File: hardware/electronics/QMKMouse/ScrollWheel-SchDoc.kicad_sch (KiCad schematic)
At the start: 8 parts

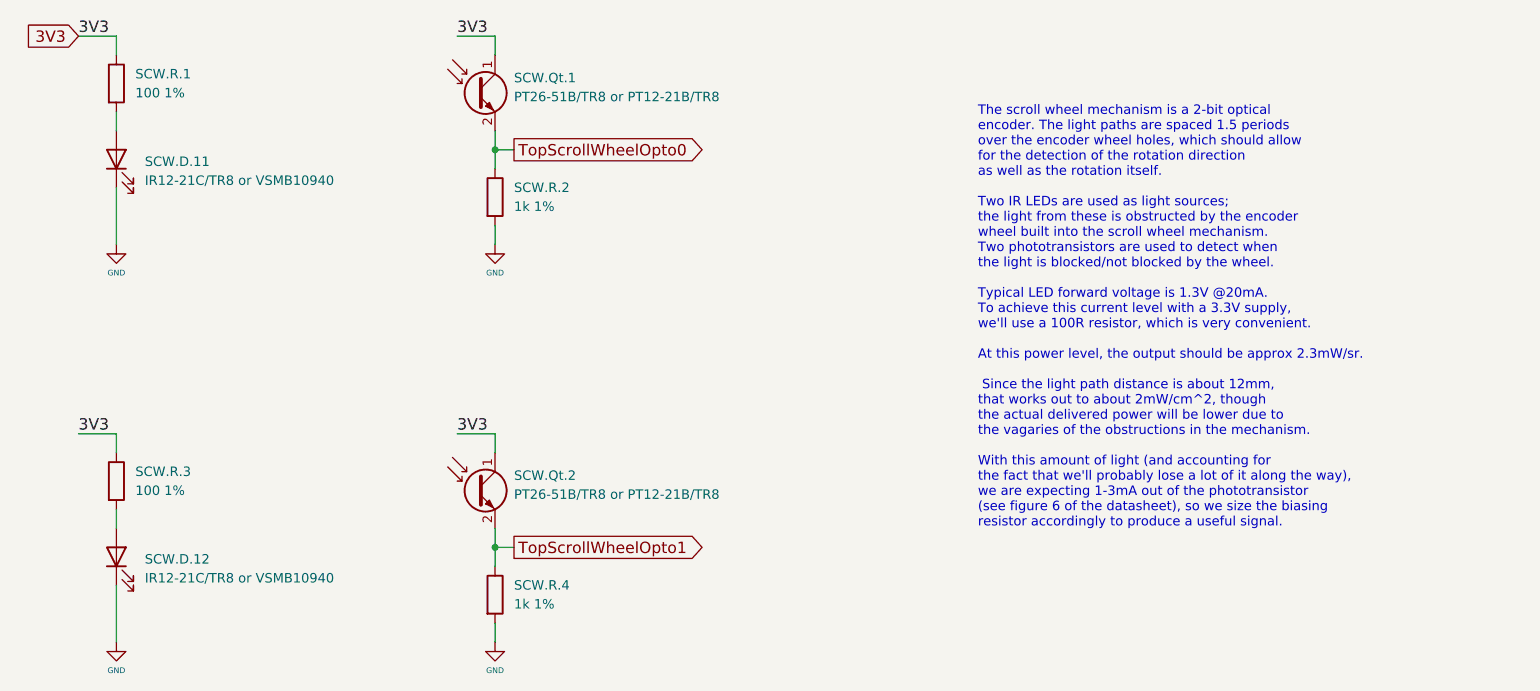
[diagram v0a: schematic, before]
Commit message: update schematic from PCB; sync netlist and fix some symbol orientations; also fix LED symbol
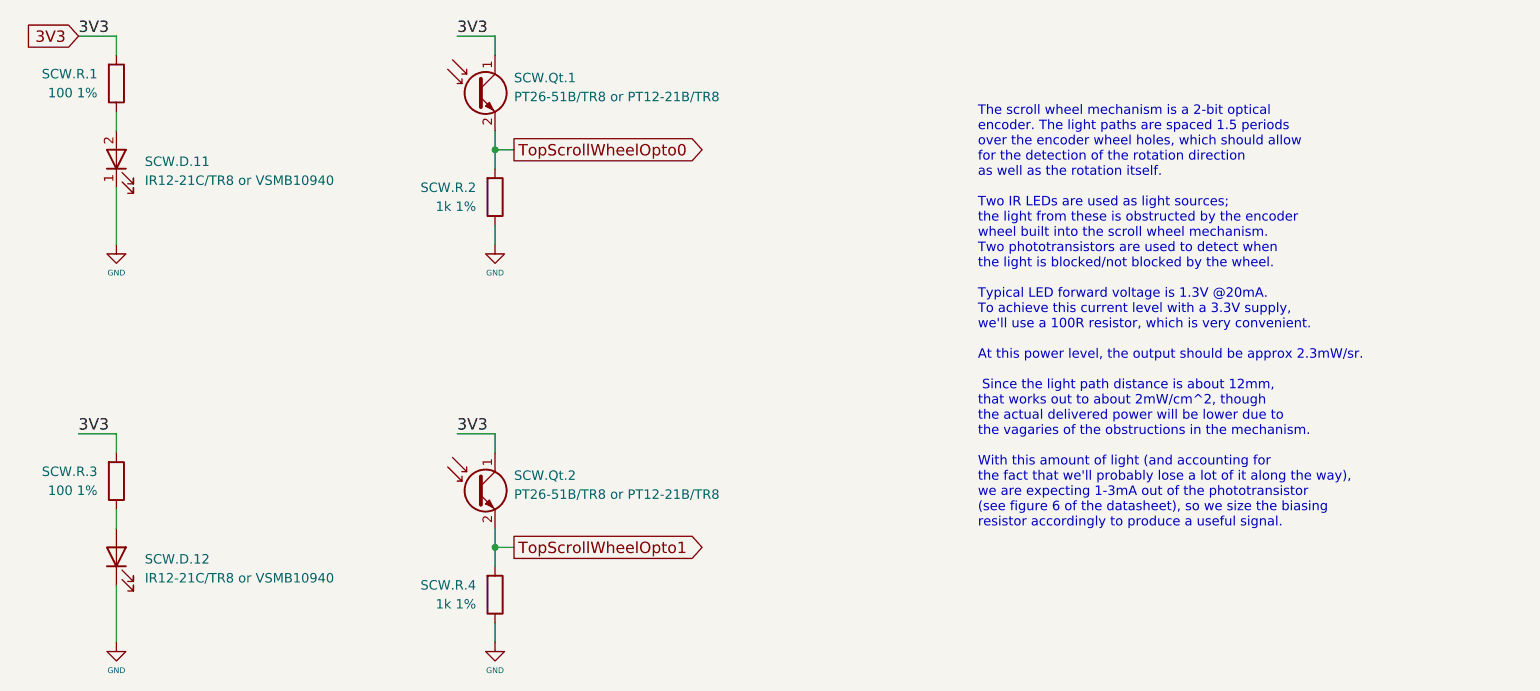
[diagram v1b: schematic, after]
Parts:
- SCW.D.11, SCW.D.12: footprint Mouse_Parts:Infrared emitter - VSMB10940 -> LEDs.PcbLib:IR12-21C/TR8
- SCW.Qt.1, SCW.Qt.2: footprint Mouse_Parts:Photo transistor - PT12-21B-TR8 -> OptoElectronics.PcbLib:PT26-51B/TR8
- SCW.R.1, SCW.R.2, SCW.R.3, SCW.R.4: footprint Resistor_SMD:R_0805_2012Metric -> Chip_Passives.PcbLib:0805
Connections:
- net 3V3: now also SCW.R.1.2, SCW.R.3.2; no longer SCW.R.1.1, SCW.R.3.1
- net GND: now also SCW.R.2.1, SCW.R.4.1; no longer SCW.R.2.2, SCW.R.4.2
- net TopScrollWheelOpto0: now also SCW.R.2.2; no longer SCW.R.2.1
- net TopScrollWheelOpto1: now also SCW.R.4.2; no longer SCW.R.4.1
- net at SCW.D.12.2 (A): now also SCW.R.3.1; no longer SCW.R.3.2
- net at SCW.D.11.2 (A): now also SCW.R.1.1; no longer SCW.R.1.2
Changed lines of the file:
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@@
     (pin "1")
   )
-  (symbol (lib_id "Device:R") (at 82.55 116.84 0) (unit 1)
+  (symbol (lib_id "Device:R") (at 82.55 116.84 0) (mirror x) (unit 1)
     (in_bom yes) (on_board yes) (fields_autoplaced)
-    (property "Reference" "SCW.R.3" (id 0) (at 85.09 115.5699 0)
-      (effects (font (size 1.27 1.27)) (justify left))
+    (property "Reference" "SCW.R.3" (id 0) (at 80.01 115.5699 0)
+      (effects (font (size 1.27 1.27)) (justify right))
     )
-    (property "Value" "100 1%" (id 1) (at 85.09 118.1099 0)
-      (effects (font (size 1.27 1.27)) (justify left))
+    (property "Value" "100 1%" (id 1) (at 80.01 118.1099 0)
+      (effects (font (size 1.27 1.27)) (justify right))
     )
-    (property "Footprint" "Resistor_SMD:R_0805_2012Metric" (id 2) (at 80.772 116.84 90)
+    (property "Footprint" "Chip_Passives.PcbLib:0805" (id 2) (at 80.772 116.84 90)
       (effects (font (size 1.27 1.27)) hide)
     )
@@
       (effects (font (size 1.27 1.27)) (justify right))
     )
-    (property "Footprint" "Mouse_Parts:Infrared emitter - VSMB10940" (id 2) (at 82.55 127 0)
+    (property "Footprint" "LEDs.PcbLib:IR12-21C{slash}TR8" (id 2) (at 82.55 127 0)
       (effects (font (size 1.27 1.27)) hide)
     )
@@
       (effects (font (size 1.27 1.27)) (justify left))
     )
-    (property "Footprint" "Mouse_Parts:Photo transistor - PT12-21B-TR8" (id 2) (at 135.89 115.57 0)
+    (property "Footprint" "OptoElectronics.PcbLib:PT26-51B{slash}TR8" (id 2) (at 135.89 115.57 0)
       (effects (font (size 1.27 1.27)) hide)
     )
@@
     (pin "2")
   )
-  (symbol (lib_id "Device:R") (at 82.55 63.5 0) (unit 1)
+  (symbol (lib_id "Device:R") (at 82.55 63.5 0) (mirror x) (unit 1)
     (in_bom yes) (on_board yes) (fields_autoplaced)
-    (property "Reference" "SCW.R.1" (id 0) (at 85.09 62.2299 0)
-      (effects (font (size 1.27 1.27)) (justify left))
+    (property "Reference" "SCW.R.1" (id 0) (at 80.01 62.2299 0)
+      (effects (font (size 1.27 1.27)) (justify right))
     )
-    (property "Value" "100 1%" (id 1) (at 85.09 64.7699 0)
-      (effects (font (size 1.27 1.27)) (justify left))
+    (property "Value" "100 1%" (id 1) (at 80.01 64.7699 0)
+      (effects (font (size 1.27 1.27)) (justify right))
     )
-    (property "Footprint" "Resistor_SMD:R_0805_2012Metric" (id 2) (at 80.772 63.5 90)
+    (property "Footprint" "Chip_Passives.PcbLib:0805" (id 2) (at 80.772 63.5 90)
       (effects (font (size 1.27 1.27)) hide)
     )
@@
     (pin "2")
   )
-  (symbol (lib_id "Device:LED") (at 82.55 73.66 90) (unit 1)
+  (symbol (lib_name "LED_1") (lib_id "Device:LED") (at 82.55 73.66 90) (unit 1)
     (in_bom yes) (on_board yes) (fields_autoplaced)
     (property "Reference" "SCW.D.11" (id 0) (at 86.36 73.9774 90)
@@
       (effects (font (size 1.27 1.27)) (justify right))
     )
-    (property "Footprint" "Mouse_Parts:Infrared emitter - VSMB10940" (id 2) (at 82.55 73.66 0)
+    (property "Footprint" "LEDs.PcbLib:IR12-21C{slash}TR8" (id 2) (at 82.55 73.66 0)
       (effects (font (size 1.27 1.27)) hide)
     )
@@
     (pin "2")
   )
-  (symbol (lib_id "Device:R") (at 133.35 132.08 0) (unit 1)
+  (symbol (lib_id "Device:R") (at 133.35 132.08 0) (mirror x) (unit 1)
     (in_bom yes) (on_board yes) (fields_autoplaced)
-    (property "Reference" "SCW.R.4" (id 0) (at 135.89 130.8099 0)
-      (effects (font (size 1.27 1.27)) (justify left))
+    (property "Reference" "SCW.R.4" (id 0) (at 130.81 130.8099 0)
+      (effects (font (size 1.27 1.27)) (justify right))
     )
-    (property "Value" "1k 1%" (id 1) (at 135.89 133.3499 0)
-      (effects (font (size 1.27 1.27)) (justify left))
+    (property "Value" "1k 1%" (id 1) (at 130.81 133.3499 0)
+      (effects (font (size 1.27 1.27)) (justify right))
     )
-    (property "Footprint" "Resistor_SMD:R_0805_2012Metric" (id 2) (at 131.572 132.08 90)
+    (property "Footprint" "Chip_Passives.PcbLib:0805" (id 2) (at 131.572 132.08 90)
       (effects (font (size 1.27 1.27)) hide)
     )
@@
     (pin "2")
   )
-  (symbol (lib_id "Device:R") (at 133.35 78.74 0) (unit 1)
+  (symbol (lib_id "Device:R") (at 133.35 78.74 0) (mirror x) (unit 1)
     (in_bom yes) (on_board yes) (fields_autoplaced)
-    (property "Reference" "SCW.R.2" (id 0) (at 135.89 77.4699 0)
-      (effects (font (size 1.27 1.27)) (justify left))
+    (property "Reference" "SCW.R.2" (id 0) (at 130.81 77.4699 0)
+      (effects (font (size 1.27 1.27)) (justify right))
     )
-    (property "Value" "1k 1%" (id 1) (at 135.89 80.0099 0)
-      (effects (font (size 1.27 1.27)) (justify left))
+    (property "Value" "1k 1%" (id 1) (at 130.81 80.0099 0)
+      (effects (font (size 1.27 1.27)) (justify right))
     )
-    (property "Footprint" "Resistor_SMD:R_0805_2012Metric" (id 2) (at 131.572 78.74 90)
+    (property "Footprint" "Chip_Passives.PcbLib:0805" (id 2) (at 131.572 78.74 90)
       (effects (font (size 1.27 1.27)) hide)
     )
@@
       (effects (font (size 1.27 1.27)) (justify left))
     )
-    (property "Footprint" "Mouse_Parts:Photo transistor - PT12-21B-TR8" (id 2) (at 135.89 62.23 0)
+    (property "Footprint" "OptoElectronics.PcbLib:PT26-51B{slash}TR8" (id 2) (at 135.89 62.23 0)
       (effects (font (size 1.27 1.27)) hide)
     )

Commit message: fix last sync errors
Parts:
- SCW.D.11, SCW.D.12: footprint LEDs.PcbLib:IR12-21C/TR8 -> LEDs.PcbLib:IR12-21C-TR8
- SCW.Qt.1, SCW.Qt.2: footprint OptoElectronics.PcbLib:PT26-51B/TR8 -> OptoElectronics.PcbLib:PT26-51B-TR8
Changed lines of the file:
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@@
       (effects (font (size 1.27 1.27)) (justify right))
     )
-    (property "Footprint" "LEDs.PcbLib:IR12-21C{slash}TR8" (id 2) (at 82.55 127 0)
+    (property "Footprint" "LEDs.PcbLib:IR12-21C-TR8" (id 2) (at 82.55 127 0)
       (effects (font (size 1.27 1.27)) hide)
     )
@@
       (effects (font (size 1.27 1.27)) (justify left))
     )
-    (property "Footprint" "OptoElectronics.PcbLib:PT26-51B{slash}TR8" (id 2) (at 135.89 115.57 0)
+    (property "Footprint" "OptoElectronics.PcbLib:PT26-51B-TR8" (id 2) (at 135.89 115.57 0)
       (effects (font (size 1.27 1.27)) hide)
     )
@@
       (effects (font (size 1.27 1.27)) (justify right))
     )
-    (property "Footprint" "LEDs.PcbLib:IR12-21C{slash}TR8" (id 2) (at 82.55 73.66 0)
+    (property "Footprint" "LEDs.PcbLib:IR12-21C-TR8" (id 2) (at 82.55 73.66 0)
       (effects (font (size 1.27 1.27)) hide)
     )
@@
       (effects (font (size 1.27 1.27)) (justify left))
     )
-    (property "Footprint" "OptoElectronics.PcbLib:PT26-51B{slash}TR8" (id 2) (at 135.89 62.23 0)
+    (property "Footprint" "OptoElectronics.PcbLib:PT26-51B-TR8" (id 2) (at 135.89 62.23 0)
       (effects (font (size 1.27 1.27)) hide)
     )

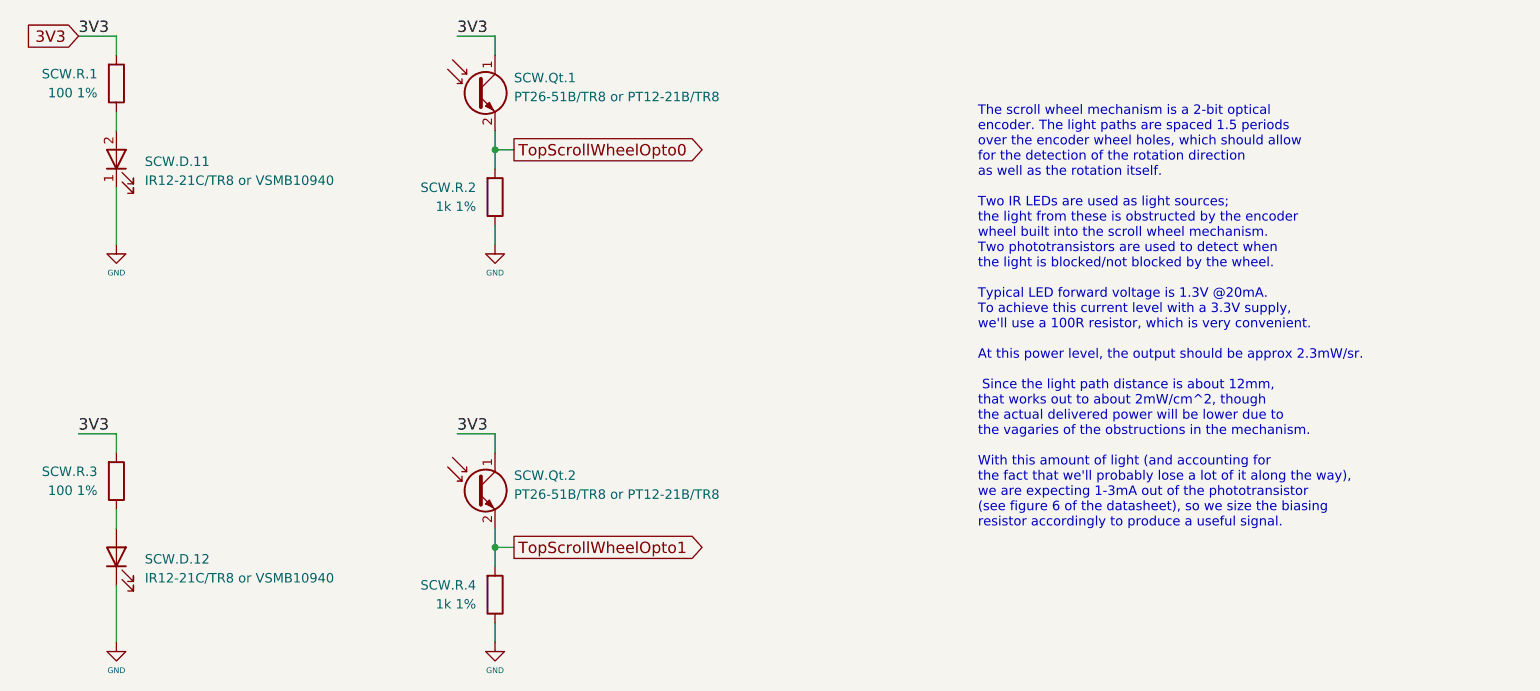
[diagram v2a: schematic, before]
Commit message: fix ERC errors and use hierarchy labels
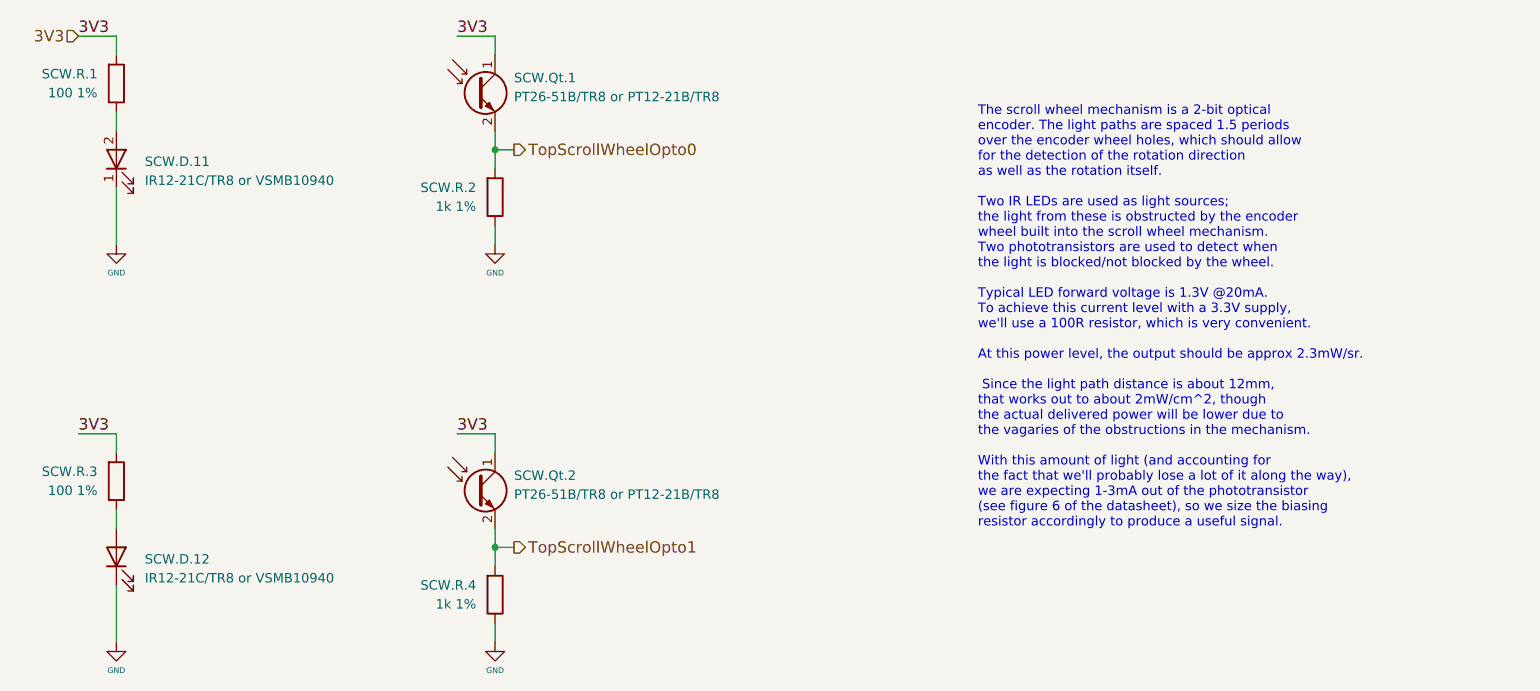
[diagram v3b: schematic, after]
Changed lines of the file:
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@@
     (effects (font (size 1.524 1.524)) (justify left bottom))
   )
-  (global_label "3V3" (shape input) (at 77.47 57.15 180) (fields_autoplaced)
+  (hierarchical_label "TopScrollWheelOpto1" (shape output) (at 135.89 125.73 0)
+    (effects (font (size 1.524 1.524)) (justify left))
+  )
+  (hierarchical_label "3V3" (shape input) (at 77.47 57.15 180)
     (effects (font (size 1.524 1.524)) (justify right))
-    (property "Intersheet References" "${INTERSHEET_REFS}" (id 0) (at 163.83 -67.31 0)
-      (effects (font (size 1.27 1.27)) (justify left) hide)
-    )
   )
-  (global_label "TopScrollWheelOpto1" (shape output) (at 135.89 125.73 0) (fields_autoplaced)
+  (hierarchical_label "TopScrollWheelOpto0" (shape output) (at 135.89 72.39 0)
     (effects (font (size 1.524 1.524)) (justify left))
-    (property "Intersheet References" "${INTERSHEET_REFS}" (id 0) (at -19.05 -67.31 0)
-      (effects (font (size 1.27 1.27)) hide)
-    )
-  )
-  (global_label "TopScrollWheelOpto0" (shape output) (at 135.89 72.39 0) (fields_autoplaced)
-    (effects (font (size 1.524 1.524)) (justify left))
-    (property "Intersheet References" "${INTERSHEET_REFS}" (id 0) (at -19.05 -67.31 0)
-      (effects (font (size 1.27 1.27)) hide)
-    )
   )
   (symbol (lib_id "power:GND") (at 133.35 138.43 0) (unit 1)

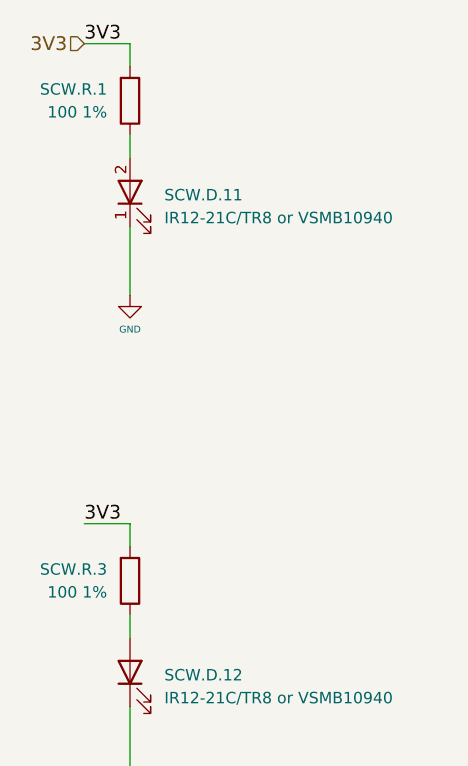
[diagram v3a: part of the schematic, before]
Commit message: Fix capacitor value and streamline resistor value naming
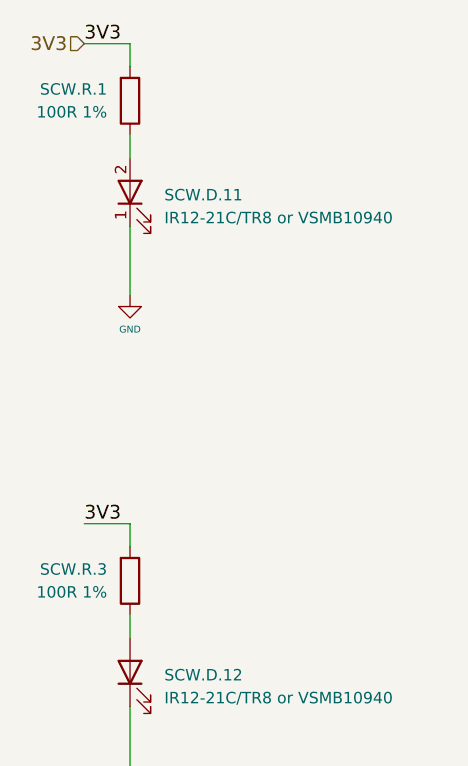
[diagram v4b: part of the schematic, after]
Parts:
- SCW.R.1, SCW.R.3: value 100 1% -> 100R 1%
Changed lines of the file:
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@@
       (effects (font (size 1.27 1.27)) (justify right))
     )
-    (property "Value" "100 1%" (id 1) (at 80.01 118.1099 0)
+    (property "Value" "100R 1%" (id 1) (at 80.01 118.1099 0)
       (effects (font (size 1.27 1.27)) (justify right))
     )
@@
       (effects (font (size 1.27 1.27)) (justify right))
     )
-    (property "Value" "100 1%" (id 1) (at 80.01 64.7699 0)
+    (property "Value" "100R 1%" (id 1) (at 80.01 64.7699 0)
       (effects (font (size 1.27 1.27)) (justify right))
     )

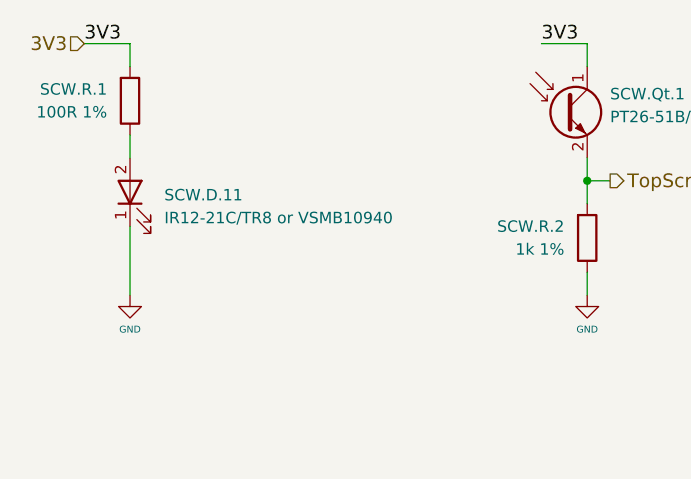
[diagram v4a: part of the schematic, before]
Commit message: correct 2 resistor values and further improve BoM (BoM matches Altium BoM now)
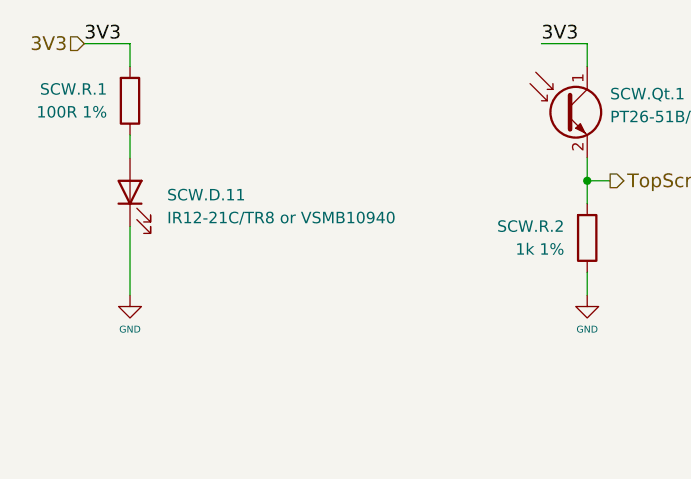
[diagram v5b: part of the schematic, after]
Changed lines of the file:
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@@
     (pin "1")
+  )
+  (symbol (lib_id "Device:LED") (at 82.55 73.66 90) (unit 1)
+    (in_bom yes) (on_board yes) (fields_autoplaced)
+    (property "Reference" "SCW.D.11" (id 0) (at 86.67 73.9774 90)
+      (effects (font (size 1.27 1.27)) (justify right))
+    )
+    (property "Value" "IR12-21C/TR8 or VSMB10940 " (id 1) (at 86.67 76.5174 90)
+      (effects (font (size 1.27 1.27)) (justify right))
+    )
+    (property "Footprint" "LEDs.PcbLib:IR12-21C-TR8" (id 2) (at 82.55 73.66 0)
+      (effects (font (size 1.27 1.27)) hide)
+    )
+    (property "Datasheet" "~" (id 3) (at 82.55 73.66 0)
+      (effects (font (size 1.27 1.27)) hide)
+    )
+    (pin "1")
+    (pin "2")
   )
   (symbol (lib_id "Device:R") (at 82.55 116.84 0) (mirror x) (unit 1)
@@
       (effects (font (size 1.27 1.27)) hide)
     )
-    (pin "1")
-    (pin "2")
-  )
-  (symbol (lib_name "LED_1") (lib_id "Device:LED") (at 82.55 73.66 90) (unit 1)
-    (in_bom yes) (on_board yes) (fields_autoplaced)
-    (property "Reference" "SCW.D.11" (id 0) (at 86.36 73.9774 90)
-      (effects (font (size 1.27 1.27)) (justify right))
-    )
-    (property "Value" "IR12-21C/TR8 or VSMB10940 " (id 1) (at 86.36 76.5174 90)
-      (effects (font (size 1.27 1.27)) (justify right))
-    )
-    (property "Footprint" "LEDs.PcbLib:IR12-21C-TR8" (id 2) (at 82.55 73.66 0)
-      (effects (font (size 1.27 1.27)) hide)
-    )
-    (property "Datasheet" "~" (id 3) (at 82.55 73.66 0)
-      (effects (font (size 1.27 1.27)) hide)
-    )
